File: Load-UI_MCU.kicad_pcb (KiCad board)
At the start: 4 copper layers, 85 x 90 mm, 110 parts, among them IC1 MSPM0G3519SPMR, IC2 TPS73533DRVT, IC3 TC4429CPA, IC4 TPS2121RUXR, J1 Conn_01x05_Socket, J10 Conn_01x02_Socket, J11 Conn_01x02_Socket, J12 Conn_01x02_Socket, J13 Conn_01x02_Socket, J14 Conn_01x02_Socket, J15 Conn_01x08_Pin, J16 Conn_01x02_Socket, J19 Conn_01x03_Socket, J2 Conn_01x06_Socket, J20 Conn_01x02_Socket, J21 Conn_01x02_Socket, J22 Conn_01x02_Socket, J23 Conn_01x02_Socket, J24 Conn_01x02_Socket, J3 Conn_01x02_Socket, J4 Conn_01x06_Socket, J5 Conn_01x02_Socket, J6 Conn_01x02_Socket, J7 Conn_01x02_Socket, J8 Conn_01x06_Socket, J9 Conn_01x03_Socket, Q2 2N2219, SW1 SW_Push, SW2 SW_Push, SW3 SW_Push_DPDT, U1 INA229AQDGSRQ1, U2 INA229AQDGSRQ1, U3 SN74HC14N, U4 SN74HC14N

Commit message: Changed NRST button silkscreen
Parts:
- renumbered SW1 to NRST
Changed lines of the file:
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@@
 		(descr "Generic 6mm SW tactile push button")
 		(tags "tact sw push 6mm")
-		(property "Reference" "SW1"
+		(property "Reference" "NRST"
 			(at 3.25 -2 0)
 			(layer "F.SilkS")

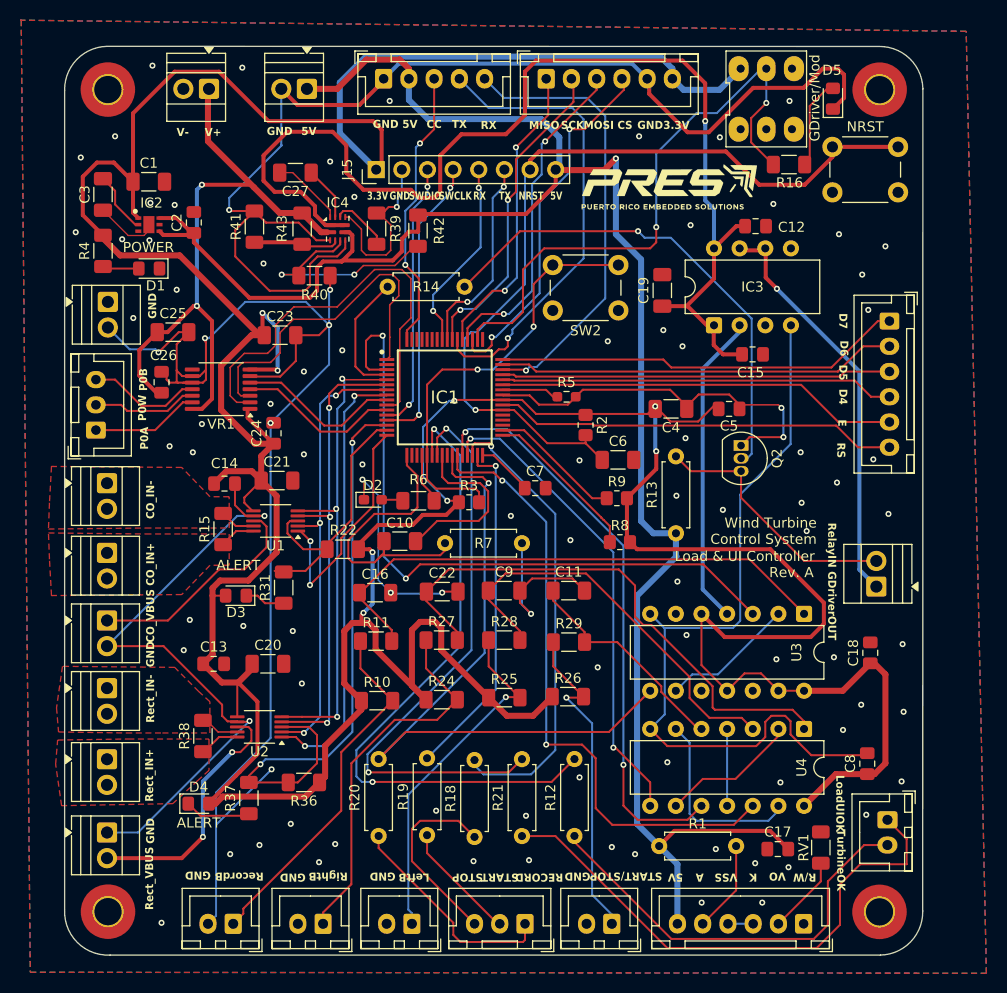
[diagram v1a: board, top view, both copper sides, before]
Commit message: removed unnecessary vias
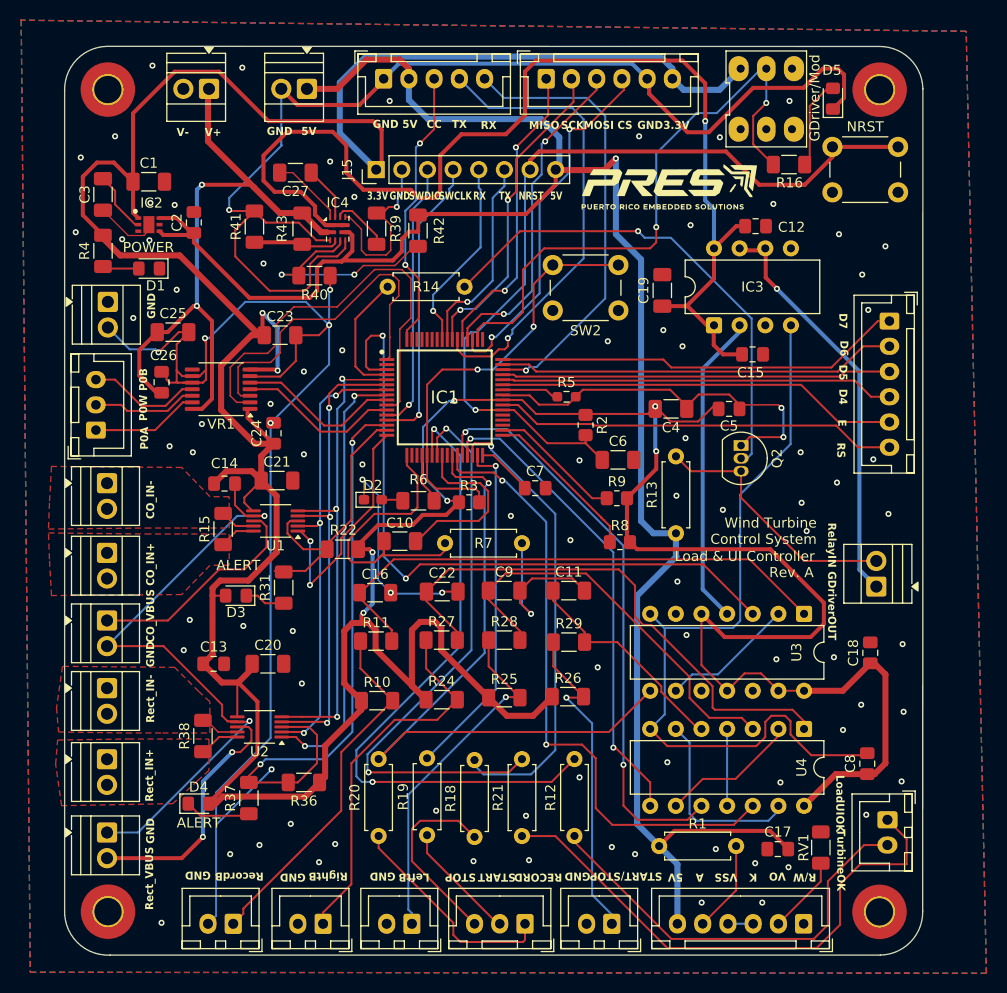
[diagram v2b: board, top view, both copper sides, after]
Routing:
- net SWDCLK: vias 2 -> 1
- net UART0_TX_XDS: vias 2 -> 1
- net UART0_RX_XDS: vias 2 -> 1
- net SWDIO: vias 2 -> 1
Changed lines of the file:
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@@
 	)
 	(gr_text "STOP"
-		(at 156.9 132.3 180)
+		(at 156.2 132.3 180)
 		(layer "F.SilkS")
 		(effects
@@
 	)
 	(gr_text "GND"
-		(at 125.7 75.7 90)
+		(at 125.6 75.7 90)
 		(layer "F.SilkS")
 		(effects
@@
 	)
 	(gr_text "START"
-		(at 160.1 132.3 180)
+		(at 159.8 132.3 180)
 		(layer "F.SilkS")
 		(effects
@@
 	)
 	(gr_text "RECORD"
-		(at 164 132.3 180)
+		(at 163.9 132.3 180)
 		(layer "F.SilkS")
 		(effects
@@
 	)
 	(gr_text "P0W"
-		(at 124.7 85.8 90)
+		(at 124.8 85.8 90)
 		(layer "F.SilkS")
 		(effects
@@
 	)
 	(segment
-		(start 158.02 64)
-		(end 158.02 62.2)
-		(width 0.2)
-		(layer "F.Cu")
-		(net 27)
-	)
-	(segment
 		(start 154.4 77.1)
 		(end 153.5 76.2)
@@
 	)
 	(via
-		(at 158.02 64)
-		(size 0.6)
-		(drill 0.3)
-		(layers "F.Cu" "B.Cu")
-		(net 27)
-	)
-	(via
 		(at 153.5 76.2)
 		(size 0.6)
@@
 	)
 	(segment
+		(start 158.02 64)
+		(end 158.02 62.2)
+		(width 0.2)
+		(layer "B.Cu")
+		(net 27)
+	)
+	(segment
 		(start 176.29816 81.012)
 		(end 177.08616 81.8)
@@
 		(net 39)
 	)
-	(segment
-		(start 152.94 63.9)
-		(end 152.94 62.2)
-		(width 0.2)
-		(layer "F.Cu")
-		(net 39)
-	)
-	(via
-		(at 152.94 63.9)
-		(size 0.6)
-		(drill 0.3)
-		(layers "F.Cu" "B.Cu")
-		(net 39)
-	)
 	(via
 		(at 151.1 85.5)
@@
 	(segment
 		(start 151.5 85.1)
-		(end 151.1 85.5)
+		(end 151.5 66.1)
 		(width 0.2)
 		(layer "B.Cu")
@@
 	)
 	(segment
-		(start 152.94 63.9)
-		(end 152.94 64.66)
+		(start 151.1 85.5)
+		(end 151.5 85.1)
 		(width 0.2)
 		(layer "B.Cu")
@@
 	)
 	(segment
-		(start 151.5 66.1)
-		(end 151.5 85.1)
+		(start 152.94 64.66)
+		(end 152.94 62.2)
 		(width 0.2)
 		(layer "B.Cu")
@@
 	)
 	(segment
-		(start 152.94 64.66)
-		(end 151.5 66.1)
+		(start 151.5 66.1)
+		(end 152.94 64.66)
 		(width 0.2)
 		(layer "B.Cu")
@@
 	)
 	(segment
-		(start 155.2 64)
-		(end 155.48 63.72)
-		(width 0.2)
-		(layer "F.Cu")
-		(net 41)
-	)
-	(segment
 		(start 151.588 87.012)
 		(end 148.912 87.012)
@@
 		(net 41)
 	)
-	(segment
-		(start 155.48 63.72)
-		(end 155.48 62.2)
-		(width 0.2)
-		(layer "F.Cu")
-		(net 41)
-	)
 	(via
 		(at 152.1 86.5)
@@
 		(net 41)
 	)
-	(via
-		(at 155.2 64)
-		(size 0.6)
-		(drill 0.3)
-		(layers "F.Cu" "B.Cu")
+	(segment
+		(start 152.1 67.6)
+		(end 155.1 64.6)
+		(width 0.2)
+		(layer "B.Cu")
 		(net 41)
 	)
 	(segment
 		(start 155.1 64.1)
-		(end 155.1 64.6)
+		(end 155.48 63.72)
 		(width 0.2)
 		(layer "B.Cu")
@@
 	)
 	(segment
-		(start 155.2 64)
-		(end 155.1 64.1)
+		(start 155.48 63.72)
+		(end 155.48 62.2)
 		(width 0.2)
 		(layer "B.Cu")
@@
 	)
 	(segment
-		(start 155.1 64.6)
+		(start 152.1 86.5)
 		(end 152.1 67.6)
 		(width 0.2)
@@
 	)
 	(segment
-		(start 152.1 67.6)
-		(end 152.1 86.5)
+		(start 155.1 64.6)
+		(end 155.1 64.1)
 		(width 0.2)
 		(layer "B.Cu")
@@
 		(net 43)
 	)
-	(segment
-		(start 160.56 62.2)
-		(end 160.56 63.84)
-		(width 0.2)
-		(layer "F.Cu")
-		(net 43)
-	)
-	(segment
-		(start 160.56 63.84)
-		(end 160.5 63.9)
-		(width 0.2)
-		(layer "F.Cu")
-		(net 43)
-	)
 	(via
-		(at 160.5 63.9)
+		(at 156.9 75.3)
 		(size 0.6)
 		(drill 0.3)
@@
 		(net 43)
 	)
-	(via
-		(at 156.9 75.3)
-		(size 0.6)
-		(drill 0.3)
-		(layers "F.Cu" "B.Cu")
+	(segment
+		(start 160.56 63.84)
+		(end 160.56 62.2)
+		(width 0.2)
+		(layer "B.Cu")
 		(net 43)
 	)
 	(segment
-		(start 159.4 65)
-		(end 160.5 63.9)
+		(start 156.9 75.3)
+		(end 157.3 75.3)
 		(width 0.2)
 		(layer "B.Cu")
@@
 	)
 	(segment
-		(start 156.9 75.3)
-		(end 157.3 75.3)
+		(start 159.4 65)
+		(end 160.56 63.84)
 		(width 0.2)
 		(layer "B.Cu")
@@
 	)
 	(segment
-		(start 185 57.1)
-		(end 185 59.5)
-		(width 0.2)
-		(layer "F.Cu")
-		(net 111)
-	)
-	(segment
 		(start 162.4 72.1)
 		(end 164.5 70)
@@
 	)
 	(segment
+		(start 186.5 55.6)
+		(end 185.2 56.9)
+		(width 0.2)
+		(layer "F.Cu")
+		(net 111)
+	)
+	(segment
 		(start 158.5345 77.4)
 		(end 161.3 77.4)
@@
 	)
 	(segment
+		(start 185.2 59.7)
+		(end 187.2 61.7)
+		(width 0.2)
+		(layer "F.Cu")
+		(net 111)
+	)
+	(segment
 		(start 157.9 78.0345)
 		(end 158.5345 77.4)
@@
 	)
 	(segment
-		(start 175.6 69.4)
-		(end 175.6 67.9)
-		(width 0.2)
-		(layer "F.Cu")
-		(net 111)
-	)
-	(segment
-		(start 186.5 55.6)
-		(end 185 57.1)
+		(start 185.2 56.9)
+		(end 185.2 59.7)
 		(width 0.2)
 		(layer "F.Cu")
@@
 	)
 	(segment
-		(start 185 59.5)
-		(end 187.2 61.7)
+		(start 175.6 69.4)
+		(end 175.6 67.9)
 		(width 0.2)
 		(layer "F.Cu")

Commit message: Added final changes to PCB: 1. Fixed OV2 ressitors on Power MUX, 2. Added input filtering on both INA229, 3. Changed the LDO layout based on manufacturer recomendations.
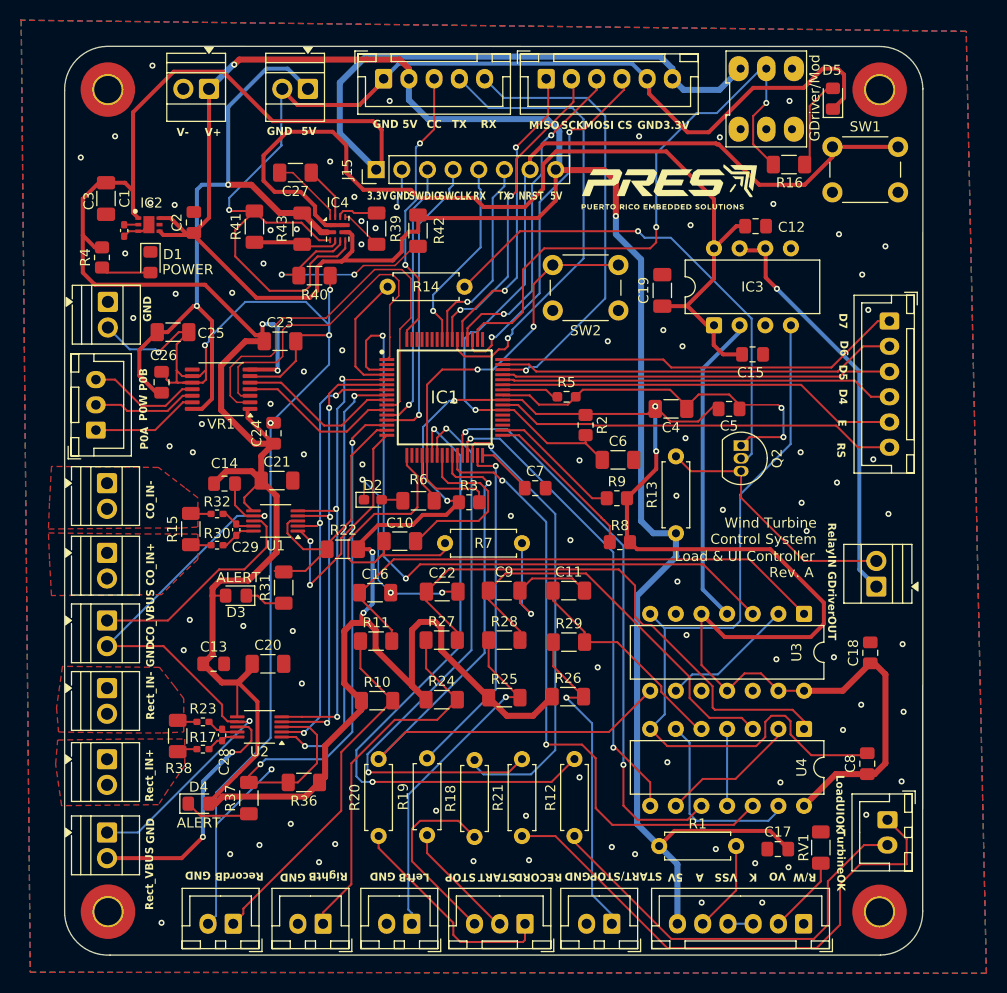
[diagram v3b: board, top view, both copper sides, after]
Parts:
- added C28: 100n, Capacitor_SMD:C_0402_1005Metric_Pad0.74x0.62mm_HandSolder, F.Cu at (132.6, 118.2)
- added C29: 100n, Capacitor_SMD:C_0402_1005Metric_Pad0.74x0.62mm_HandSolder, F.Cu at (134.0, 97.9)
- added R17: 50, Resistor_SMD:R_0402_1005Metric_Pad0.72x0.64mm_HandSolder, F.Cu at (130.7, 119.6)
- added R23: 50, Resistor_SMD:R_0402_1005Metric_Pad0.72x0.64mm_HandSolder, F.Cu at (130.7, 116.9)
- added R30: 50, Resistor_SMD:R_0402_1005Metric_Pad0.72x0.64mm_HandSolder, F.Cu at (132.1, 99.4)
- added R32: 50, Resistor_SMD:R_0402_1005Metric_Pad0.72x0.64mm_HandSolder, F.Cu at (132.1, 96.3)
- C3: footprint Capacitor_SMD:C_1206_3216Metric_Pad1.33x1.80mm_HandSolder -> Capacitor_SMD:C_0402_1005Metric_Pad0.74x0.62mm_HandSolder
- R4: footprint Resistor_SMD:R_1206_3216Metric_Pad1.30x1.75mm_HandSolder -> Resistor_SMD:R_0805_2012Metric_Pad1.20x1.40mm_HandSolder
- R43: value 23.7k -> 100k
- moved J11 9.80 mm to (141.1, 54.2)
- moved J10 9.70 mm to (131.3, 54.2)
- moved C1 4.55 mm to (121.1, 65.1), turned to -90 degrees
- moved C3 4.14 mm to (122.9, 68.2)
- moved R15 3.20 mm to (129.5, 97.8)
- moved R38 2.50 mm to (128.2, 118.3)
- moved R4 0.66 mm to (120.7, 70.9)
- moved D1 0.64 mm to (125.5, 71.4), turned to -90 degrees
- moved C23 0.60 mm to (138.3, 79.2)
- turned R39 to -90 degrees
- renumbered NRST to SW1
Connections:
- IC2 pad 3: GNDA -> GND
- U1 pad 10: ConverterOUT_IN+ -> Net-(U1-IN+)
- U1 pad 9: ConverterOUT_IN- -> Net-(U1-IN-)
- U2 pad 10: Rectifier_IN+ -> Net-(U2-IN+)
- U2 pad 9: Rectifier_IN- -> Net-(U2-IN-)
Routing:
- net +5V: track 197.7 -> 220.6 mm, vias 1 -> 2
- net Highest_Power_Supply: track 112.0 -> 95.5 mm, vias 1 -> 0
- net GND: track 501.8 -> 488.9 mm, vias 99 -> 102
- net External_Power_Supply: track 63.0 -> 69.4 mm
- net Net-(IC2-NR): track 6.18 -> 1.41 mm
- net Net-(U1-IN+): track 0.00 -> 3.58 mm
- net Net-(U2-IN-): track 0.00 -> 3.53 mm
- net Net-(U1-IN-): track 0.00 -> 3.50 mm
- net Net-(U2-IN+): track 0.00 -> 3.44 mm
- net Rectifier_IN+: track 4.18 -> 2.17 mm
- net Rectifier_IN-: track 4.54 -> 2.67 mm
- net ConverterOUT_IN+: track 3.59 -> 2.03 mm
- net ConverterOUT_IN-: track 3.52 -> 2.03 mm
- net Net-(D1-A): track 3.92 -> 5.15 mm
- net NRST: track 84.1 -> 85.0 mm
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
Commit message: Finished pcb for manufacturing, changed some footprints based on what the manufacturer had. Also I fixed the potentiometer footprint.
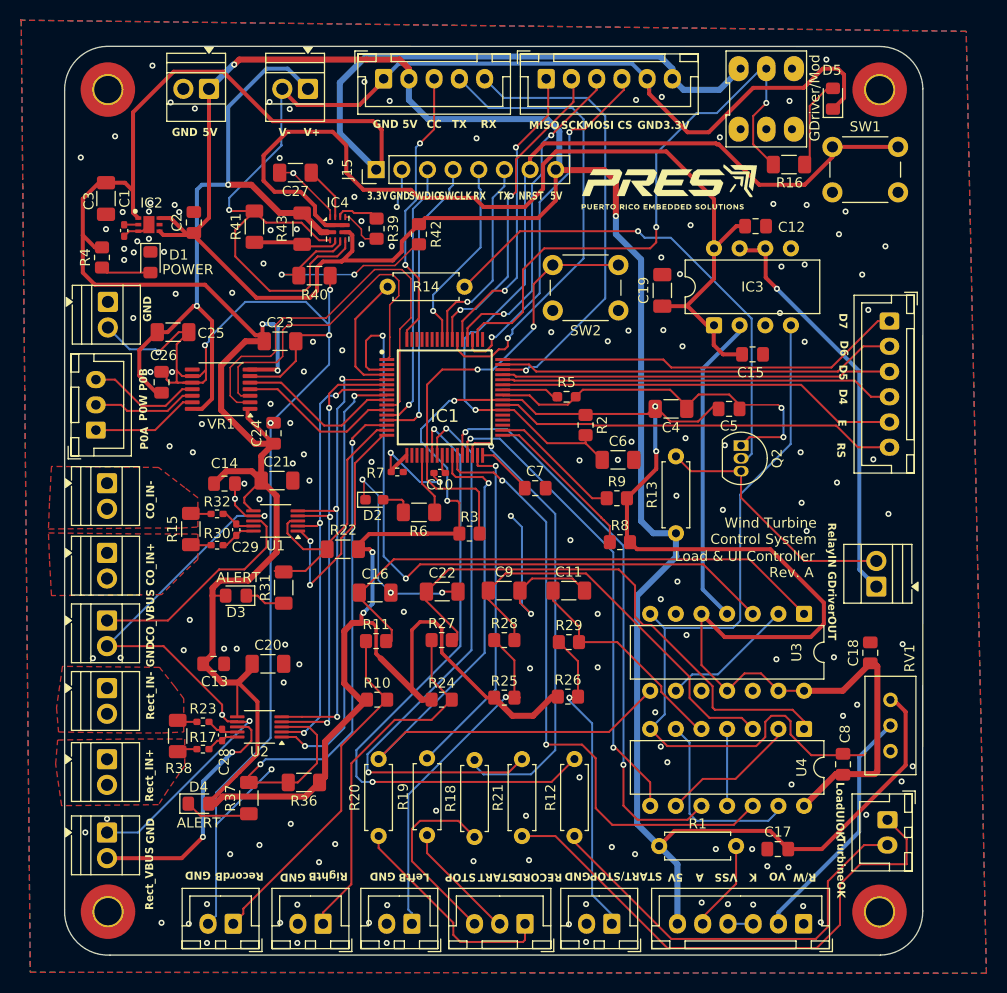
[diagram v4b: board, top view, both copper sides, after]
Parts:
- C10: footprint Capacitor_SMD:C_1206_3216Metric_Pad1.33x1.80mm_HandSolder -> Capacitor_SMD:C_0402_1005Metric_Pad0.74x0.62mm_HandSolder
- C11, C9: value 4.7uF -> 4.7u
- C16: value 4.7k -> 4.7u; footprint Resistor_SMD:R_1206_3216Metric_Pad1.30x1.75mm_HandSolder -> Capacitor_SMD:C_1206_3216Metric_Pad1.33x1.80mm_HandSolder
- C18, C8: value 100nF -> 100n
- R10, R11, R24, R25, R26, R27, R28, R29: footprint Resistor_SMD:R_1206_3216Metric_Pad1.30x1.75mm_HandSolder -> Resistor_SMD:R_0805_2012Metric_Pad1.20x1.40mm_HandSolder
- R39: value 51.1k -> 51k; footprint Resistor_SMD:R_1206_3216Metric_Pad1.30x1.75mm_HandSolder -> Resistor_SMD:R_0805_2012Metric_Pad1.20x1.40mm_HandSolder
- R40, R41: value 5k -> 4.7k
- R42: value 23.7k -> 24k; footprint Resistor_SMD:R_1206_3216Metric_Pad1.30x1.75mm_HandSolder -> Resistor_SMD:R_0805_2012Metric_Pad1.20x1.40mm_HandSolder
- R7: footprint Resistor_THT:R_Axial_DIN0207_L6.3mm_D2.5mm_P7.62mm_Horizontal -> Resistor_SMD:R_0402_1005Metric_Pad0.72x0.64mm_HandSolder
- RV1: footprint Resistor_SMD:R_1206_3216Metric_Pad1.30x1.75mm_HandSolder -> Potentiometer_THT:Potentiometer_Bourns_3296W_Vertical
- moved RV1 11.8 mm to (198.8, 119.8)
- moved R7 8.49 mm to (149.9, 92.2)
- moved C10 7.82 mm to (154.2, 92.2)
- moved R3 3.10 mm to (157.1, 98.2)
- moved C8 2.40 mm to (194.1, 121.1)
- moved R6 1.15 mm to (152.1, 96.2)
- moved R42 0.36 mm to (152.1, 68.6)
- moved D2 0.15 mm to (147.7, 94.9)
- moved R10 0.10 mm to (147.9, 114.7)
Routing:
- net +5V: track 220.6 -> 242.0 mm
- net Net-(IC1-PA21_/_A1_7_/_VREF-): track 28.6 -> 11.4 mm, vias 0 -> 2
- net Net-(J4-Pin_2): track 7.74 -> 24.2 mm
- net Net-(IC1-PA23_VREF+): track 18.0 -> 1.88 mm
- net Net-(IC1-PB22): track 42.5 -> 45.7 mm
- net GND: track 488.9 -> 492.0 mm, vias 102 -> 172
- net +3.3V: track 458.3 -> 460.2 mm
- net START/STOP_BUTTON : track 32.6 -> 31.2 mm
- net Net-(D2-A): track 2.28 -> 3.31 mm
- net RIGHT_BUTTON : track 37.4 -> 36.3 mm
- net Net-(IC1-PB21): track 5.20 -> 6.17 mm
- net RECORD_BUTTON: track 35.9 -> 35.2 mm
- net Net-(IC4-ILIM): track 4.88 -> 4.33 mm

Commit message: EE
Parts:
- added G***: LOGO, LOGO, F.Cu at (154.7, 84.8)
